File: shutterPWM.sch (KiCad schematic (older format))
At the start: 25 parts, among them P11 2x3 header strip R/A, P12 2x3 header strip R/A, U2 DRV103, U3 DRV103, U4 MCP4728

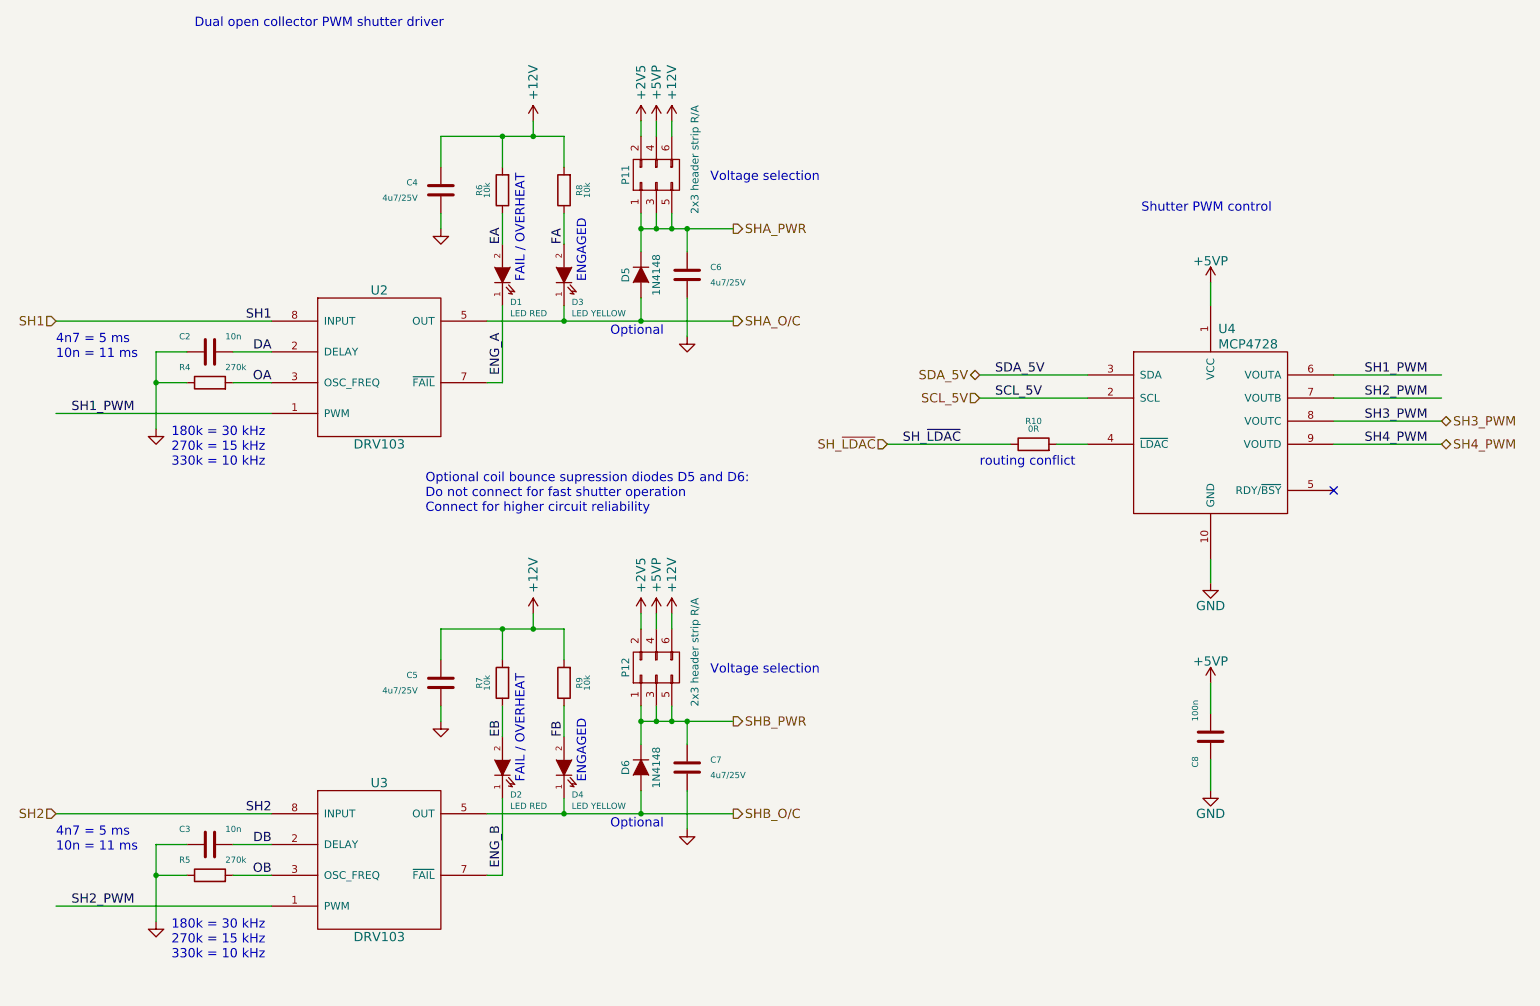
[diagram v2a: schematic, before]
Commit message: Changed ENGAGED LED anode to +5V, changed SOD-323 packages.
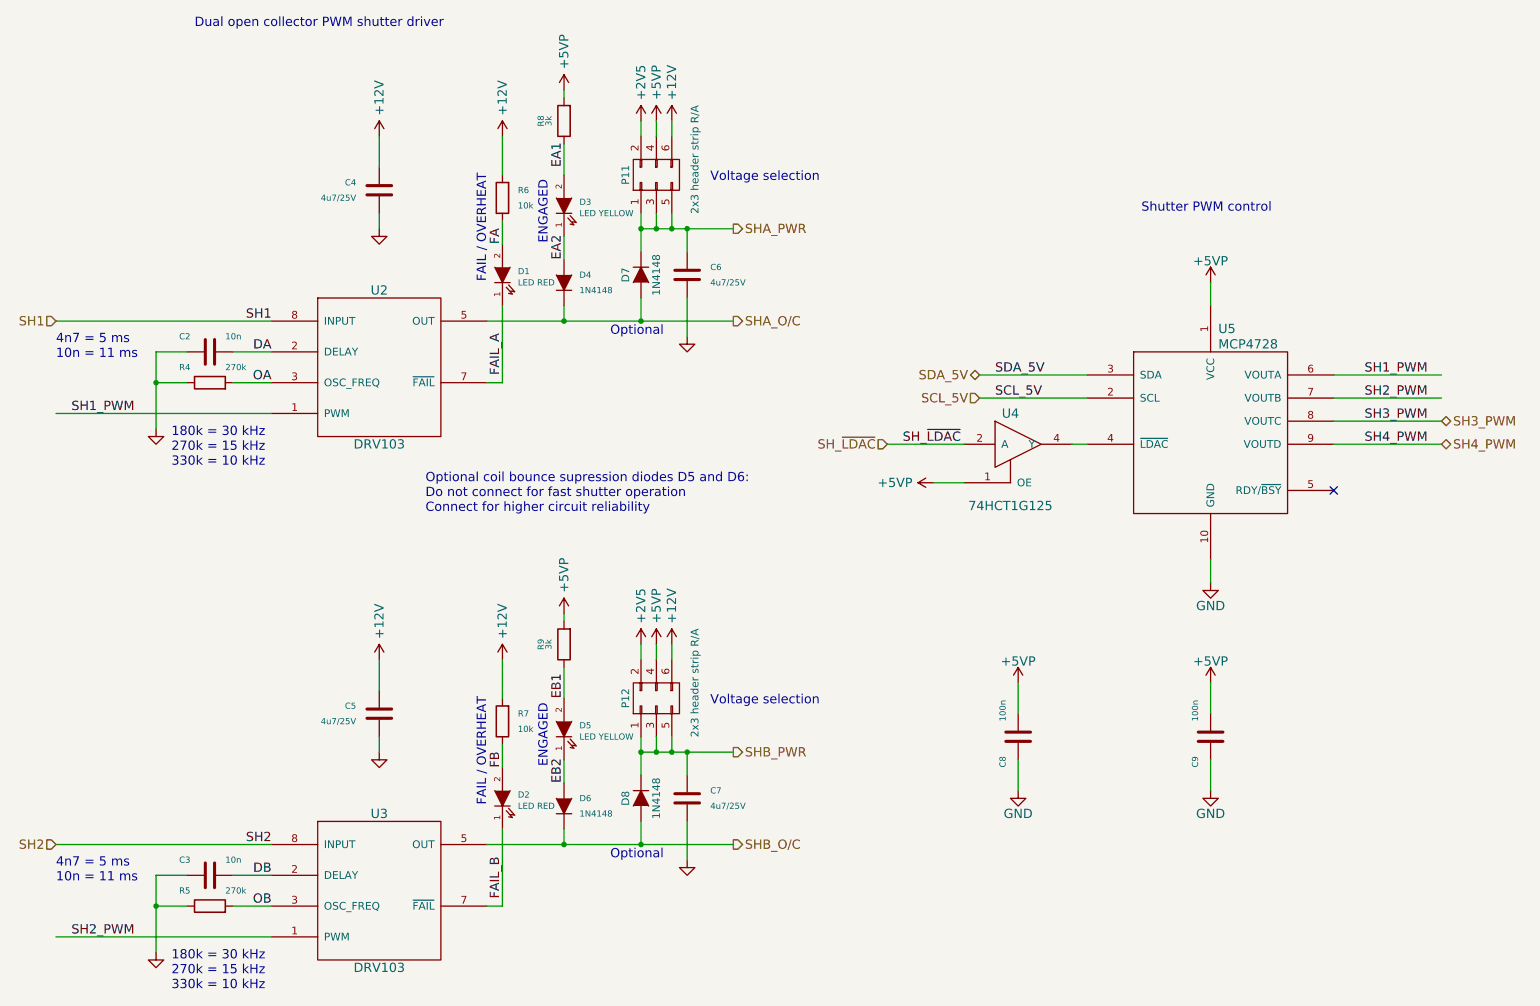
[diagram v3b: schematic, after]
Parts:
- removed D4: LED YELLOW, LEDs:LED-1206, symbol LED
- removed R10: 0R, Resistors_SMD:R_0805, symbol R
- added C8: 100n, Capacitors_SMD:C_0805, symbol C
- added D4, D6: 1N4148, jakub:SOD-323, symbol D
- added D5: LED YELLOW, LEDs:LED-1206, symbol LED
- added U4: 74HCT1G125, TO_SOT_Packages_SMD:SOT-23-5, symbol 74HCT1G125
- D1, D2: Manufacturer Lumex -> Broadcom
- D3: Manufacturer Avago -> Broadcom
- D7: renamed from D5; footprint Diodes_SMD:SOD-323 -> jakub:SOD-323
- D8: renamed from D6; footprint Diodes_SMD:SOD-323 -> jakub:SOD-323
- R8, R9: value 10k -> 3k; Alt. Order Code 71-CRCW0805-10K-E3 -> 667-ERJ-6GEYJ302V; Note 10kΩ/1% 0805 resistor -> 3kΩ/1% 0805 resistor; Order Code 2073607 -> 9332995; Part Number MCMR08X1002FTL -> MC01W080513K
- renumbered C8 to C9, U4 to U5
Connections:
- net labels added: EA1, EA2, EB1, EB2, FAIL_A, FAIL_B
- net labels removed: EA, EB, ENG_A, ENG_B
- wire segments 70 -> 71
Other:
- note removed: "routing conflict"
- moved on the sheet: C3, C4, C7, D3, D8, P12, R5, U3
